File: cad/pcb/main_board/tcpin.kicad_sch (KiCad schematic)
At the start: 3 parts

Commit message: Add Aisler files
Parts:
- R3, R4: footprint (none) -> Resistor_SMD:R_0805_2012Metric
- TC1: footprint (none) -> Connector_PinSocket_2.54mm:PinSocket_1x02_P2.54mm_Vertical
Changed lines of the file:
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@@
       (effects (font (size 1.27 1.27)) (justify right))
     )
-    (property "Footprint" "" (at 92.71 95.885 0)
+    (property "Footprint" "Connector_PinSocket_2.54mm:PinSocket_1x02_P2.54mm_Vertical" (at 92.71 95.885 0)
       (effects (font (size 1.27 1.27)) hide)
     )
@@
       (effects (font (size 1.27 1.27)) (justify right))
     )
-    (property "Footprint" "" (at 95.758 69.85 90)
+    (property "Footprint" "Resistor_SMD:R_0805_2012Metric" (at 95.758 69.85 90)
       (effects (font (size 1.27 1.27)) hide)
     )
@@
       (effects (font (size 1.27 1.27)) (justify right))
     )
-    (property "Footprint" "" (at 95.758 59.69 90)
+    (property "Footprint" "Resistor_SMD:R_0805_2012Metric" (at 95.758 59.69 90)
       (effects (font (size 1.27 1.27)) hide)
     )

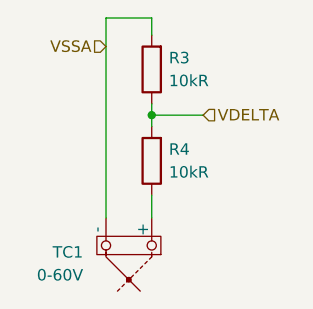
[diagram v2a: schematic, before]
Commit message: Organizing Thermo Couple Connections
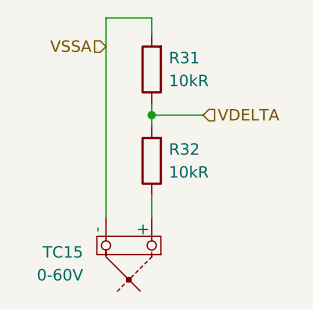
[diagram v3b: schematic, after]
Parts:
- renumbered R3 to R31, R4 to R32, TC1 to TC15
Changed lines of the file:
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@@
 		(on_board yes)
 		(dnp no)
-		(property "Reference" "TC1"
+		(property "Reference" "TC15"
 			(at 86.36 80.01 90)
 			(effects
@@
 		(on_board yes)
 		(dnp no)
-		(property "Reference" "R4"
+		(property "Reference" "R32"
 			(at 95.885 68.58 0)
 			(effects
@@
 		(on_board yes)
 		(dnp no)
-		(property "Reference" "R3"
+		(property "Reference" "R31"
 			(at 95.885 58.42 0)
 			(effects

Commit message: Hooking up ThermoCouple pins first layout of TCs
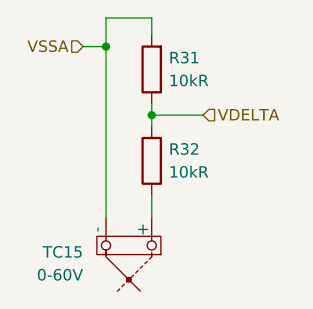
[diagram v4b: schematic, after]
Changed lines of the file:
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@@
+		(color 0 0 0 0)
+	)
+	(junction
+		(at 88.9 57.15)
+		(diameter 0)
 		(color 0 0 0 0)
 	)
@@
 	(wire
 		(pts
-			(xy 88.9 53.975) (xy 88.9 76.2)
+			(xy 88.9 57.15) (xy 88.9 76.2)
+		)
+		(stroke
+			(width 0)
+			(type default)
+		)
+	)
+	(wire
+		(pts
+			(xy 88.9 53.975) (xy 88.9 57.15)
 		)
 		(stroke
@@
 		(pts
 			(xy 93.98 63.5) (xy 93.98 64.77)
+		)
+		(stroke
+			(width 0)
+			(type default)
+		)
+	)
+	(wire
+		(pts
+			(xy 86.36 57.15) (xy 88.9 57.15)
 		)
 		(stroke
@@
 	(hierarchical_label "VSSA"
 		(shape input)
-		(at 88.9 57.15 180)
+		(at 86.36 57.15 180)
 		(fields_autoplaced yes)
 		(effects

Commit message: Adding JTAG Interface + POGO Pads
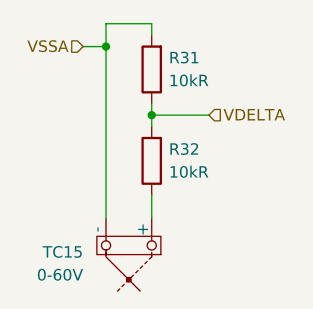
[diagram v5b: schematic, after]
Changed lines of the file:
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@@
 	(wire
 		(pts
-			(xy 93.98 64.77) (xy 99.695 64.77)
+			(xy 93.98 64.77) (xy 100.33 64.77)
 		)
 		(stroke
@@
 	(wire
 		(pts
-			(xy 88.9 53.975) (xy 88.9 57.15)
+			(xy 88.9 54.61) (xy 88.9 57.15)
 		)
 		(stroke
@@
 	(wire
 		(pts
-			(xy 93.98 53.975) (xy 88.9 53.975)
-		)
-		(stroke
-			(width 0)
-			(type default)
-		)
-	)
-	(wire
-		(pts
-			(xy 93.98 55.88) (xy 93.98 53.975)
+			(xy 93.98 54.61) (xy 88.9 54.61)
+		)
+		(stroke
+			(width 0)
+			(type default)
+		)
+	)
+	(wire
+		(pts
+			(xy 93.98 55.88) (xy 93.98 54.61)
 		)
 		(stroke
@@
 	(hierarchical_label "VDELTA"
 		(shape input)
-		(at 99.695 64.77 0)
+		(at 100.33 64.77 0)
 		(fields_autoplaced yes)
 		(effects
@@
 			)
 		)
-		(property "Description" ""
+		(property "Description" "Thermocouple with isothermal block"
 			(at 91.44 81.28 0)
 			(effects
@@
 			)
 		)
-		(property "Description" ""
+		(property "Description" "Resistor"
 			(at 93.98 69.85 0)
 			(effects
@@
 			)
 		)
-		(property "Description" ""
+		(property "Description" "Resistor"
 			(at 93.98 59.69 0)
 			(effects
